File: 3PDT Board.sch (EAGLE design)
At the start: 10 parts, among them SW2 3PDT

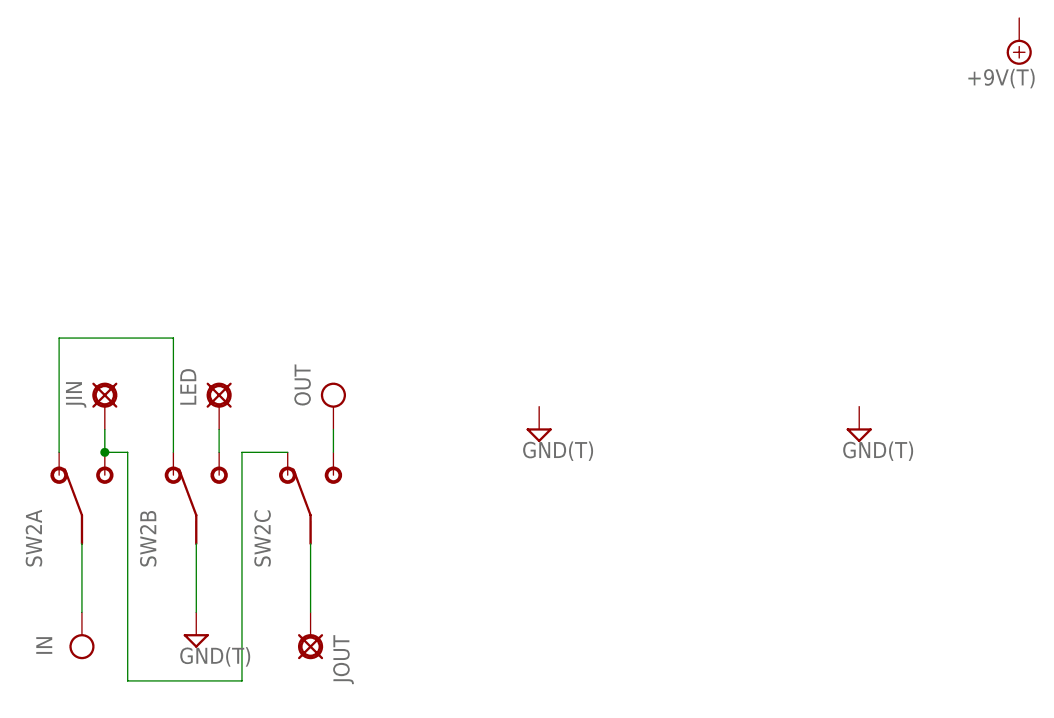
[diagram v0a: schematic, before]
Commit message: Fixed ground connections so jack grounds actually connect to ground!
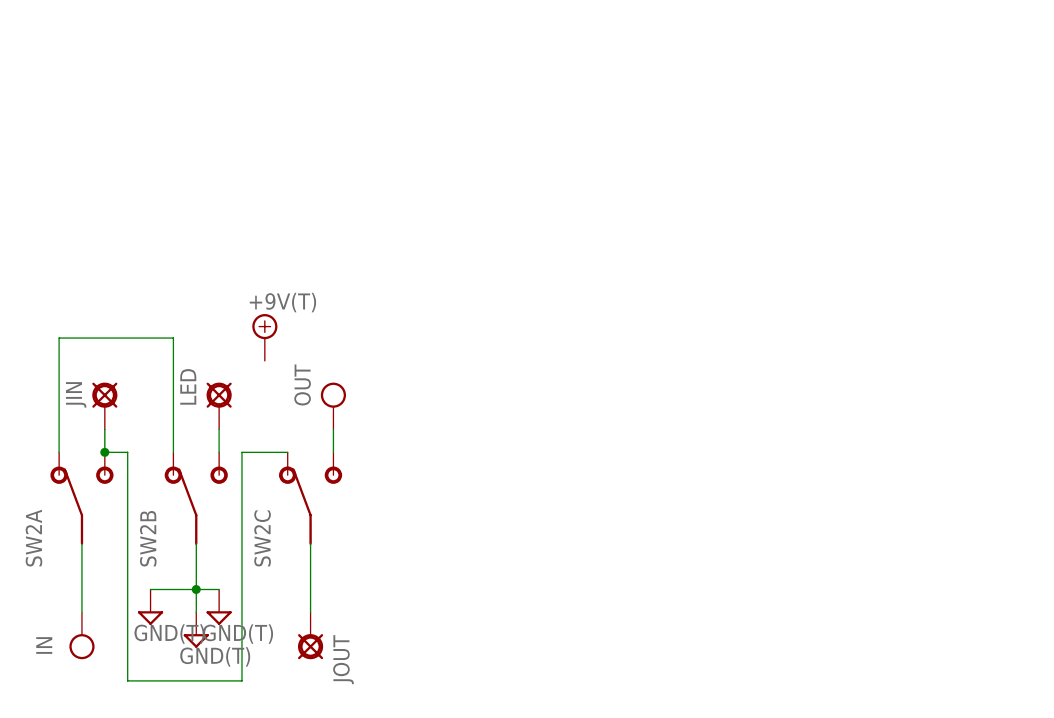
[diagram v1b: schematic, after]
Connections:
- net GND: now also JIG.GND, JOG.GND
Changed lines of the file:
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@@
 <instances>
 <instance part="G" gate="GND" x="25.4" y="12.7"/>
-<instance part="JOG" gate="GND" x="99.06" y="35.56"/>
+<instance part="JOG" gate="GND" x="20.32" y="15.24"/>
 <instance part="IN" gate="G$1" x="12.7" y="12.7" rot="R90"/>
 <instance part="OUT" gate="G$1" x="40.64" y="38.1" rot="R90"/>
 <instance part="JOUT" gate="G$1" x="38.1" y="12.7" rot="R270"/>
 <instance part="JIN" gate="G$1" x="15.24" y="38.1" rot="R90"/>
-<instance part="+9V" gate="+9V" x="116.84" y="78.74" rot="R180"/>
+<instance part="+9V" gate="+9V" x="33.02" y="45.72"/>
 <instance part="LED" gate="G$1" x="27.94" y="38.1" rot="R90"/>
-<instance part="JIG" gate="GND" x="63.5" y="35.56"/>
+<instance part="JIG" gate="GND" x="27.94" y="15.24"/>
 <instance part="SW2" gate="A" x="12.7" y="27.94"/>
 <instance part="SW2" gate="B" x="25.4" y="27.94"/>
@@
 <segment>
 <pinref part="G" gate="GND" pin="GND"/>
-<wire x1="25.4" y1="22.86" x2="25.4" y2="15.24" width="0.1524" layer="91"/>
+<wire x1="25.4" y1="22.86" x2="25.4" y2="17.78" width="0.1524" layer="91"/>
 <pinref part="SW2" gate="B" pin="2"/>
+<pinref part="JOG" gate="GND" pin="GND"/>
+<wire x1="25.4" y1="17.78" x2="25.4" y2="15.24" width="0.1524" layer="91"/>
+<wire x1="20.32" y1="17.78" x2="25.4" y2="17.78" width="0.1524" layer="91"/>
+<junction x="25.4" y="17.78"/>
+<pinref part="JIG" gate="GND" pin="GND"/>
+<wire x1="27.94" y1="17.78" x2="25.4" y2="17.78" width="0.1524" layer="91"/>
 </segment>
 </net>

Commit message: Fixed circuit and made panel
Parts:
- removed IN: IN(T), mb_supply:IN(T)
- removed LED: (no value), mb_supply:PAD
- removed OUT: OUT(T), mb_supply:OUT(T)
- added D1: 1N4001, mb_diodes:1N400X.3
- added U$1: BOARDLINK, xc_library:BOARDLINK
- renumbered JOUT to JOT
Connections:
- removed net IN: IN.IN, SW2A.2
- removed net OUT: OUT.OUT, SW2C.3
- new net +9V: +9V.+9V, D1.C
- new net N$5: SW2A.2, U$1.IN
- new net N$6: SW2C.3, U$1.OUT
- new net N$7: D1.A, U$1.+9V
- net GND: now also U$1.G
- net N$1: now also U$1.LED; no longer LED.PAD
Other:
- moved on the sheet: SW2C
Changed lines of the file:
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@@
 <?xml version="1.0" encoding="utf-8"?>
 <!DOCTYPE eagle SYSTEM "eagle.dtd">
-<eagle version="8.4.1">
+<eagle version="9.1.0">
 <drawing>
 <settings>
@@
 <classes>
 <class number="0" name="default" width="0" drill="0">
+<clearance class="0" value="0.205"/>
 </class>
 </classes>
@@
 <part name="G" library="mb_supply" deviceset="GND(T)" device=""/>
 <part name="JOG" library="mb_supply" deviceset="GND(T)" device=""/>
-<part name="IN" library="mb_supply" deviceset="IN(T)" device=""/>
-<part name="OUT" library="mb_supply" deviceset="OUT(T)" device=""/>
-<part name="JOUT" library="mb_supply" deviceset="PAD" device=""/>
+<part name="JOT" library="mb_supply" deviceset="PAD" device=""/>
 <part name="JIN" library="mb_supply" deviceset="PAD" device=""/>
-<part name="+9V" library="mb_supply" deviceset="+9V(T)" device=""/>
-<part name="LED" library="mb_supply" deviceset="PAD" device=""/>
 <part name="JIG" library="mb_supply" deviceset="GND(T)" device=""/>
 <part name="SW2" library="mb_switches" deviceset="3PDT" device=""/>
+<part name="U$1" library="xc_library" deviceset="BOARDLINK" device=""/>
+<part name="+9V" library="mb_supply" deviceset="+9V(T)" device=""/>
+<part name="D1" library="mb_diodes" deviceset="1N400X" device=".3" value="1N4001"/>
 </parts>
 <sheets>
@@
 <instance part="G" gate="GND" x="25.4" y="12.7"/>
 <instance part="JOG" gate="GND" x="20.32" y="15.24"/>
-<instance part="IN" gate="G$1" x="12.7" y="12.7" rot="R90"/>
-<instance part="OUT" gate="G$1" x="40.64" y="38.1" rot="R90"/>
-<instance part="JOUT" gate="G$1" x="38.1" y="12.7" rot="R270"/>
+<instance part="JOT" gate="G$1" x="38.1" y="12.7" rot="R270"/>
 <instance part="JIN" gate="G$1" x="15.24" y="38.1" rot="R90"/>
-<instance part="+9V" gate="+9V" x="33.02" y="45.72"/>
-<instance part="LED" gate="G$1" x="27.94" y="38.1" rot="R90"/>
-<instance part="JIG" gate="GND" x="27.94" y="15.24"/>
+<instance part="JIG" gate="GND" x="35.56" y="38.1"/>
 <instance part="SW2" gate="A" x="12.7" y="27.94"/>
 <instance part="SW2" gate="B" x="25.4" y="27.94"/>
-<instance part="SW2" gate="C" x="38.1" y="27.94"/>
+<instance part="SW2" gate="C" x="38.1" y="20.32"/>
+<instance part="U$1" gate="G$1" x="27.94" y="45.72"/>
+<instance part="+9V" gate="+9V" x="45.72" y="30.48" rot="R270"/>
+<instance part="D1" gate="1" x="38.1" y="30.48"/>
 </instances>
 <busses>
 </busses>
 <nets>
-<net name="N$1" class="0">
-<segment>
-<pinref part="LED" gate="G$1" pin="PAD"/>
-<wire x1="27.94" y1="35.56" x2="27.94" y2="33.02" width="0.1524" layer="91"/>
-<pinref part="SW2" gate="B" pin="3"/>
-</segment>
-</net>
 <net name="GND" class="0">
 <segment>
@@
 <wire x1="20.32" y1="17.78" x2="25.4" y2="17.78" width="0.1524" layer="91"/>
 <junction x="25.4" y="17.78"/>
+</segment>
+<segment>
+<pinref part="U$1" gate="G$1" pin="G"/>
 <pinref part="JIG" gate="GND" pin="GND"/>
-<wire x1="27.94" y1="17.78" x2="25.4" y2="17.78" width="0.1524" layer="91"/>
-</segment>
-</net>
-<net name="IN" class="0">
-<segment>
-<pinref part="IN" gate="G$1" pin="IN"/>
-<wire x1="12.7" y1="22.86" x2="12.7" y2="15.24" width="0.1524" layer="91"/>
-<pinref part="SW2" gate="A" pin="2"/>
+<wire x1="35.56" y1="41.656" x2="35.56" y2="40.64" width="0.1524" layer="91"/>
 </segment>
 </net>
 <net name="N$2" class="0">
 <segment>
-<pinref part="JOUT" gate="G$1" pin="PAD"/>
-<wire x1="38.1" y1="22.86" x2="38.1" y2="15.24" width="0.1524" layer="91"/>
+<pinref part="JOT" gate="G$1" pin="PAD"/>
 <pinref part="SW2" gate="C" pin="2"/>
 </segment>
@@
 <pinref part="JIN" gate="G$1" pin="PAD"/>
 <wire x1="15.24" y1="35.56" x2="15.24" y2="33.02" width="0.1524" layer="91"/>
-<wire x1="35.56" y1="33.02" x2="30.48" y2="33.02" width="0.1524" layer="91"/>
-<wire x1="30.48" y1="33.02" x2="30.48" y2="7.62" width="0.1524" layer="91"/>
+<wire x1="35.56" y1="25.4" x2="30.48" y2="25.4" width="0.1524" layer="91"/>
+<wire x1="30.48" y1="25.4" x2="30.48" y2="7.62" width="0.1524" layer="91"/>
 <wire x1="30.48" y1="7.62" x2="17.78" y2="7.62" width="0.1524" layer="91"/>
 <wire x1="17.78" y1="7.62" x2="17.78" y2="33.02" width="0.1524" layer="91"/>
@@
 </segment>
 </net>
-<net name="OUT" class="0">
-<segment>
-<pinref part="OUT" gate="G$1" pin="OUT"/>
-<wire x1="40.64" y1="35.56" x2="40.64" y2="33.02" width="0.1524" layer="91"/>
+<net name="N$1" class="0">
+<segment>
+<pinref part="U$1" gate="G$1" pin="LED"/>
+<wire x1="30.48" y1="41.656" x2="30.48" y2="35.56" width="0.1524" layer="91"/>
+<wire x1="30.48" y1="35.56" x2="27.94" y2="35.56" width="0.1524" layer="91"/>
+<pinref part="SW2" gate="B" pin="3"/>
+<wire x1="27.94" y1="35.56" x2="27.94" y2="33.02" width="0.1524" layer="91"/>
+</segment>
+</net>
+<net name="N$5" class="0">
+<segment>
+<wire x1="25.4" y1="48.26" x2="7.62" y2="48.26" width="0.1524" layer="91"/>
+<wire x1="7.62" y1="48.26" x2="7.62" y2="22.86" width="0.1524" layer="91"/>
+<pinref part="SW2" gate="A" pin="2"/>
+<wire x1="7.62" y1="22.86" x2="12.7" y2="22.86" width="0.1524" layer="91"/>
+<pinref part="U$1" gate="G$1" pin="IN"/>
+<wire x1="27.94" y1="41.656" x2="25.4" y2="41.656" width="0.1524" layer="91"/>
+<wire x1="25.4" y1="41.656" x2="25.4" y2="48.26" width="0.1524" layer="91"/>
+</segment>
+</net>
+<net name="N$6" class="0">
+<segment>
+<pinref part="U$1" gate="G$1" pin="OUT"/>
+<wire x1="38.1" y1="41.656" x2="38.1" y2="40.64" width="0.1524" layer="91"/>
+<wire x1="38.1" y1="40.64" x2="53.34" y2="40.64" width="0.1524" layer="91"/>
+<wire x1="53.34" y1="40.64" x2="53.34" y2="25.4" width="0.1524" layer="91"/>
 <pinref part="SW2" gate="C" pin="3"/>
-</segment>
-</net>
+<wire x1="53.34" y1="25.4" x2="40.64" y2="25.4" width="0.1524" layer="91"/>
+</segment>
+</net>
+<net name="N$7" class="0">
+<segment>
+<pinref part="U$1" gate="G$1" pin="+9V"/>
+<pinref part="D1" gate="1" pin="A"/>
+<wire x1="33.02" y1="41.656" x2="33.02" y2="30.48" width="0.1524" layer="91"/>
+</segment>
+</net>
+<net name="+9V" class="0">
+<segment>
+<pinref part="D1" gate="1" pin="C"/>
+<pinref part="+9V" gate="+9V" pin="+9V"/>
+<wire x1="40.64" y1="30.48" x2="43.18" y2="30.48" width="0.1524" layer="91"/>
+</segment>
+</net>
